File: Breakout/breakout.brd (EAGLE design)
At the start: 53.6 x 40.5 mm, 27 parts, among them U1 TPS63001DRCT, U2 MCP73831

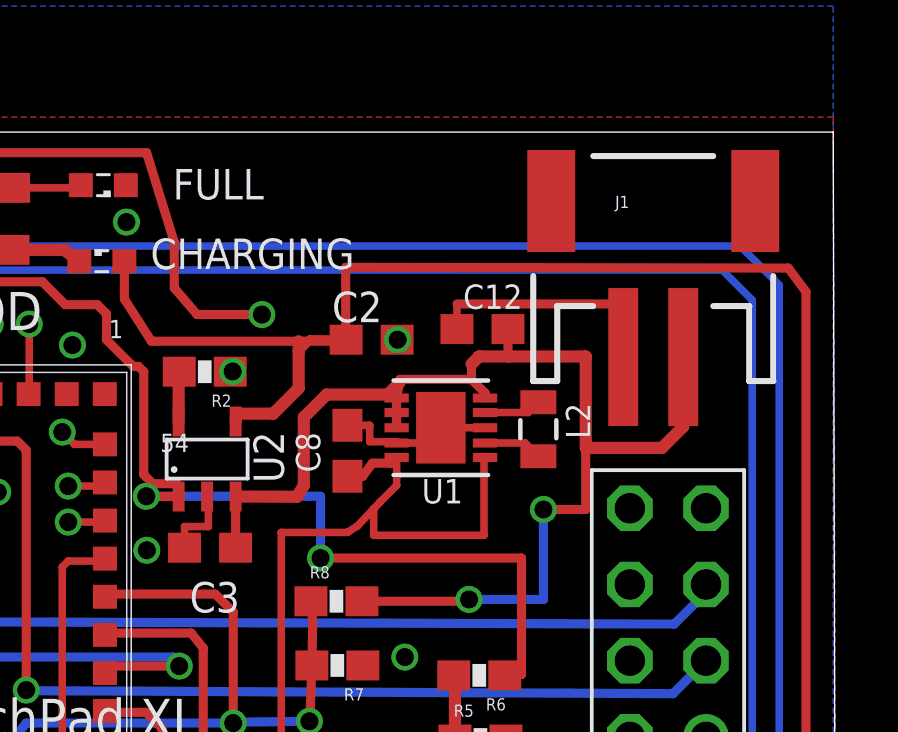
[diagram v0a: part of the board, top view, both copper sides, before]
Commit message: Fixed some pads
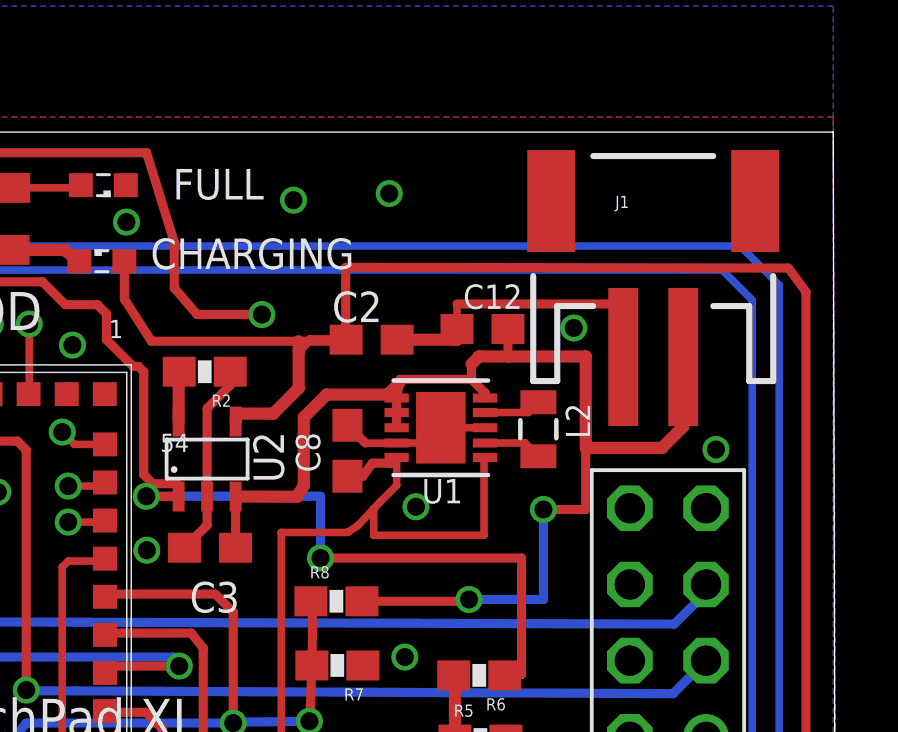
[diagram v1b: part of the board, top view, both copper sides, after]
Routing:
- net GND: track 16.8 -> 22.8 mm, vias 36 -> 39
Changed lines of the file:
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@@
 <layers>
 <layer number="1" name="Top" color="4" fill="1" visible="yes" active="yes"/>
-<layer number="2" name="Route2" color="1" fill="3" visible="yes" active="yes"/>
+<layer number="2" name="Route2" color="1" fill="3" visible="no" active="yes"/>
 <layer number="3" name="Route3" color="4" fill="3" visible="no" active="no"/>
 <layer number="14" name="Route14" color="1" fill="6" visible="no" active="no"/>
-<layer number="15" name="Route15" color="4" fill="6" visible="yes" active="yes"/>
-<layer number="16" name="Bottom" color="1" fill="1" visible="yes" active="yes"/>
+<layer number="15" name="Route15" color="4" fill="6" visible="no" active="yes"/>
+<layer number="16" name="Bottom" color="1" fill="1" visible="no" active="yes"/>
 <layer number="17" name="Pads" color="2" fill="1" visible="yes" active="yes"/>
 <layer number="18" name="Vias" color="2" fill="1" visible="yes" active="yes"/>
@@
 </polygon>
 <contactref element="FULL" pad="C"/>
-<via x="50.88" y="33.58" extent="1-16" drill="0.6"/>
 <via x="42.52" y="26.56" extent="1-16" drill="0.6"/>
 <via x="22.89" y="33.19" extent="1-16" drill="0.6"/>
@@
 <via x="41.84" y="37.5" extent="1-16" drill="0.6"/>
 <via x="37.55" y="28.5" extent="1-16" drill="0.6"/>
-<wire x1="49.206" y1="30.726" x2="49.95" y2="30.726" width="0.254" layer="1"/>
-<wire x1="49.95" y1="30.726" x2="49.95" y2="30.18" width="0.254" layer="1"/>
-<wire x1="49.95" y1="30.18" x2="50.8468" y2="30.18" width="0.254" layer="1"/>
-<wire x1="50.8468" y1="30.18" x2="50.8468" y2="30.136" width="0.254" layer="1"/>
-<via x="45.38" y="32.52" extent="1-16" drill="0.6"/>
 <wire x1="58.4" y1="33" x2="58.39" y2="34.77" width="0.254" layer="1"/>
 <wire x1="58.39" y1="34.77" x2="52.858" y2="34.77" width="0.3048" layer="1"/>
 <wire x1="52.858" y1="34.77" x2="52.858" y2="33.9342" width="0.254" layer="1"/>
-<wire x1="44.53" y1="28.3514" x2="44.57" y2="28.3514" width="0.254" layer="1"/>
-<wire x1="44.57" y1="28.3514" x2="44.57" y2="27.35" width="0.254" layer="1"/>
-<wire x1="44.57" y1="27.35" x2="43.7778" y2="27.35" width="0.254" layer="1"/>
-<wire x1="43.7778" y1="27.35" x2="43.7778" y2="26.6446" width="0.254" layer="1"/>
 <wire x1="53.7932" y1="30.644" x2="52.32" y2="30.644" width="0.254" layer="1"/>
 <via x="51.12" y="23" extent="1-16" drill="0.6"/>
 <contactref element="R5" pad="2"/>
 <contactref element="R7" pad="1"/>
+<wire x1="50.8626" y1="33.5788" x2="52.858" y2="33.5788" width="0.4064" layer="1"/>
+<wire x1="52.858" y1="33.5788" x2="52.858" y2="33.9342" width="0.4064" layer="1"/>
+<wire x1="45.3" y1="32.512" x2="45.3" y2="32.06" width="0.3048" layer="1"/>
+<wire x1="45.3" y1="32.06" x2="44.53" y2="31.29" width="0.3048" layer="1"/>
+<wire x1="44.53" y1="31.29" x2="44.53" y2="28.3514" width="0.3048" layer="1"/>
+<wire x1="49.206" y1="30.726" x2="49.214" y2="30.726" width="0.3048" layer="1"/>
+<wire x1="49.214" y1="30.726" x2="49.81" y2="30.13" width="0.3048" layer="1"/>
+<wire x1="49.81" y1="30.13" x2="50.8208" y2="30.13" width="0.254" layer="1"/>
+<wire x1="50.8208" y1="30.13" x2="50.8468" y2="30.136" width="0.254" layer="1"/>
+<wire x1="44.53" y1="28.3514" x2="44.53" y2="27.3968" width="0.3048" layer="1"/>
+<wire x1="44.53" y1="27.3968" x2="43.7778" y2="26.6446" width="0.3048" layer="1"/>
+<via x="51.49" y="28.01" extent="1-16" drill="0.6"/>
+<via x="56.75" y="33.97" extent="1-16" drill="0.6"/>
+<via x="50.6" y="38.45" extent="1-16" drill="0.6"/>
 <wire x1="41.125" y1="15.72" x2="41.89" y2="15.12" width="0" layer="19" extent="1-1"/>
-<wire x1="49.95" y1="30.726" x2="50.88" y2="33.58" width="0" layer="19" extent="1-1"/>
 <wire x1="53.506" y1="15.748" x2="54.49" y2="20.25" width="0" layer="19" extent="1-1"/>
+<via x="47.41" y="38.23" extent="1-16" drill="0.6"/>
+<via x="61.49" y="29.92" extent="1-16" drill="0.6"/>
 </signal>
 <signal name="N$1">

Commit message: Add Bom file
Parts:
- C1: value (none) -> 1pF
- L1: value (none) -> 3.6nH
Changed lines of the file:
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@@
 <element name="CC3200MOD" library="cc3200mod" package="CC3200MOD" value="CC3200" x="31.6" y="23.74"/>
 <element name="ANT_PAD" library="Antenna" package="ANT" value="ANT" x="24.65" y="0.5"/>
-<element name="C1" library="rcl" package="C0402" value="" x="26.5" y="7.6" smashed="yes">
+<element name="C1" library="rcl" package="C0402" value="1pF" x="26.5" y="7.6" smashed="yes">
 <attribute name="NAME" x="27.7192" y="7.1936" size="1.016" layer="25" font="vector" ratio="18"/>
 <attribute name="VALUE" x="25.865" y="5.695" size="1.27" layer="27"/>
 </element>
-<element name="L1" library="Spark" package="C0402" value="" x="25.9" y="11.3" smashed="yes" rot="R90">
+<element name="L1" library="Spark" package="C0402" value="3.6nH" x="25.9" y="11.3" smashed="yes" rot="R90">
 <attribute name="NAME" x="27.7923" y="11.1984" size="1.016" layer="25" font="vector" ratio="18"/>
 <attribute name="VALUE" x="27.043" y="10.2205" size="0.4064" layer="27" rot="R90"/>

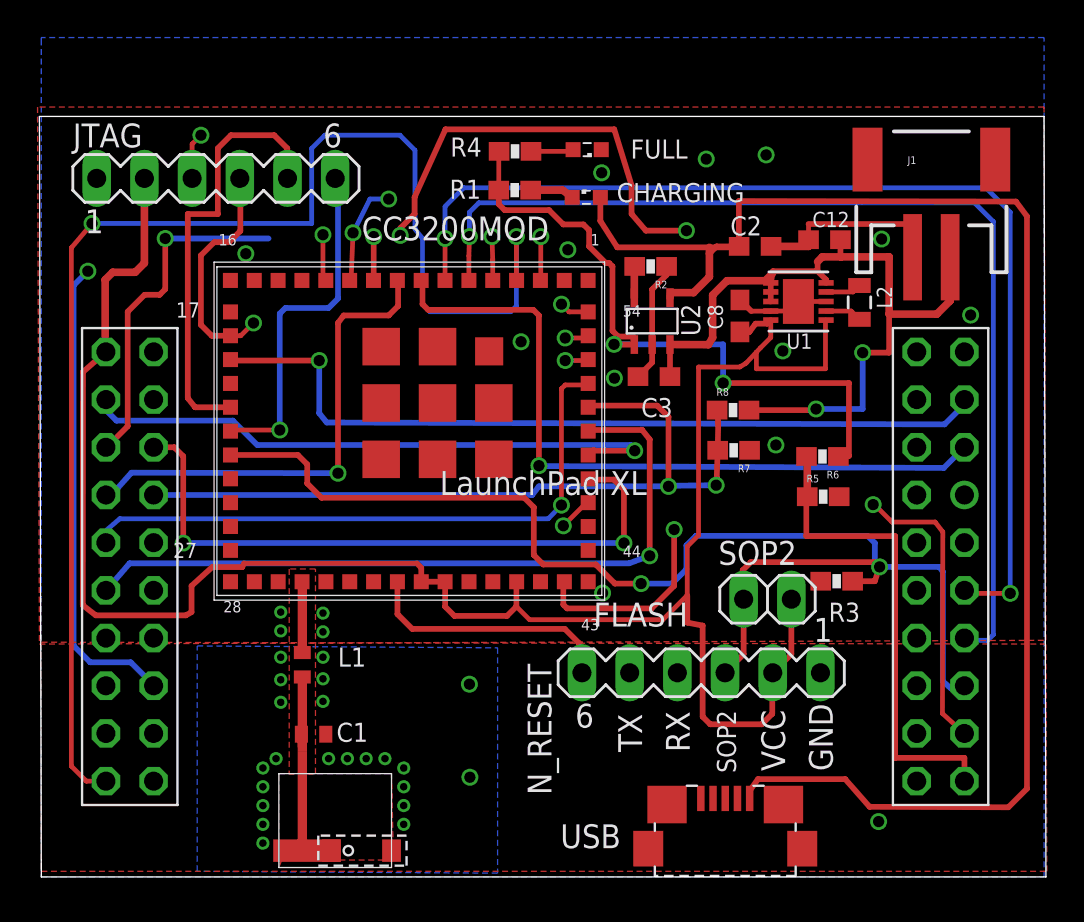
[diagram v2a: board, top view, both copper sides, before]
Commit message: switch charger
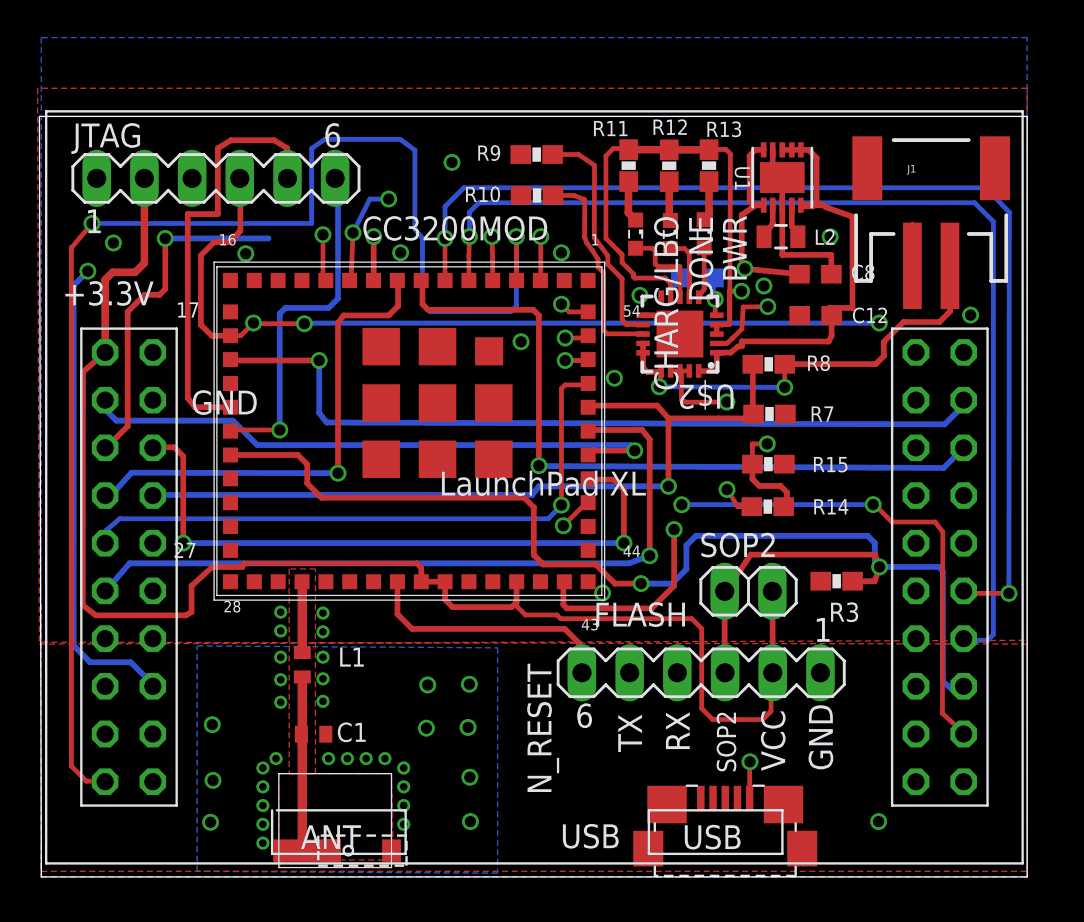
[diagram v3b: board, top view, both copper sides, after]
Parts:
- removed C2, C3: 4.7uF, rcl:C0603
- removed CHARGING, FULL: (no value), eagle-ltspice:LED_SML0603
- removed R1, R4: 470 Ohm, SparkFun-Resistors:0603-RES
- removed R2: 2 k, SparkFun-Resistors:0603-RES
- removed R5, R6: 100K, SparkFun-Resistors:0603-RES
- removed U$1: XL, LaunchPadXL:LAUNCHPADXL
- removed U2: MCP73831, BaseApp:5PIN_SOT23
- added CHARG/LBO: ORANGE, led:SML0603
- added DONE: GREEN, led:SML0603
- added PWR: RED, led:SML0603
- added R10: 100K, SparkFun-Passives:0603-RES
- added R11, R12, R13, R14, R15: 1K, SparkFun-Passives:0603-RES
- added R9: 2K, SparkFun-Passives:0603-RES
- added THERMAL: 10K, SparkFun-Passives:0603-RES
- added U$2: MCP73871-2CCI/ML, microchip-battery:QFN20-4X4
- added U11: XL, LaunchPadXL:LAUNCHPADXL
- moved U1 6.66 mm to (51.5, 37.2), turned to 90 degrees
- moved L2 5.45 mm to (51.4, 34.1), turned to 180 degrees
- moved C8 4.59 mm to (53.2, 32.1), turned to 0 degrees
- moved C12 4.06 mm to (53.2, 29.9)
- moved R8 3.09 mm to (50.7, 27.3)
- moved R7 2.72 mm to (50.8, 24.6)
- moved SOP2 1.09 mm to (49.7, 15.2)
- moved J1 0.46 mm to (59.4, 36.2)
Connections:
- removed net +5V_CHARGE: C2.1, CHARGING.A, U2.P$4, USB.1
- removed net N$7: CHARGING.C, R1.2
- removed net PROG: R2.2, U2.P$5
- removed net STAT: R1.1, R4.1, R6.1, U2.P$1
- new net +5V_USB: R11.2, R12.2, R13.2, R14.2, U$2.17, U$2.18, U$2.19, U$2.3, U$2.4, U$2.9, USB.1
- new net N$17: R9.2, U$2.12
- new net N$20: R10.2, U$2.13
- new net N$26: PWR.A, U$2.6
- new net N$31: DONE.A, U$2.7
- new net N$32: CHARG/LBO.A, U$2.8
- new net N$33: CHARG/LBO.C, R11.1
- new net N$35: DONE.C, R12.1
- new net N$36: PWR.C, R13.1
- new net N$37: R14.1, R15.2, U$2.2
- new net OUT: C12.1, U$2.1, U$2.20, U1.5, U1.6, U1.7, U1.8
- net +BATT: now also U$2.14, U$2.15, U$2.16; no longer C12.1, C3.1, U1.5, U1.6, U1.7, U1.8, U2.P$3
- net GND: now also R10.1, R15.1, R9.1, THERMAL.1, U$2.10, U$2.11, U$2.21, U11.GND1, U11.GND2; no longer C2.2, C3.2, FULL.C, R2.1, R5.2, U$1.GND1, U$1.GND2, U2.P$2
- net GPIO_05: now also U11.GPIO_05; no longer U$1.GPIO_05
- net GPIO_22: now also U11.GPIO_22; no longer R5.1, R6.2, U$1.GPIO_22
- net JTAG_TDI: now also U11.GPIO_23; no longer U$1.GPIO_23
- net JTAG_TDO: now also U11.GPIO_24; no longer U$1.GPIO_24
- net N$10: now also U11.GPIO_16_MOSI; no longer U$1.GPIO_16_MOSI
- net N$11: now also U11.GPIO_17_CS; no longer U$1.GPIO_17_CS
- net N$12: now also U11.GPIO_14_SP_CLK; no longer U$1.GPIO_14_SP_CLK
- net N$13: now also U11.GPIO_28; no longer U$1.GPIO_28
- net N$14: now also U11.GPIO_30; no longer U$1.GPIO_30
- net N$15: now also U11.GPIO_10; no longer U$1.GPIO_10
- net N$16: now also U11.GPIO_11; no longer U$1.GPIO_11
- net N$18: now also U11.GPIO_06; no longer U$1.GPIO_06
- net N$19: now also U11.GPIO_04; no longer U$1.GPIO_04
- net N$21: now also U11.GPIO_07; no longer U$1.GPIO_07
- net N$22: now also U11.GPIO_08; no longer U$1.GPIO_08
- net N$23: now also U11.GPIO_09; no longer U$1.GPIO_09
- net N$24: now also U11.GPIO_13_RX; no longer U$1.GPIO_13_RX
- net N$25: now also U11.GPIO_12_TX; no longer U$1.GPIO_12_TX
- net N$27: now also U11.GPIO_03; no longer U$1.GPIO_03
- net N$28: now also THERMAL.2, U$2.5; no longer FULL.A, R4.2
- net N$8: now also U11.GPIO_15_MISO; no longer U$1.GPIO_15_MISO
- net RX: now also U11.GPIO_01; no longer U$1.GPIO_01
- net SOP2: now also U11.GPIO_25; no longer U$1.GPIO_25
- net TX: now also U11.GPIO_02; no longer U$1.GPIO_02
- net VCC: now also U11.3.3V; no longer U$1.3.3V
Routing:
- net +5V_CHARGE: track 81.0 -> 0.00 mm
- net +5V_USB: track 0.00 -> 65.4 mm, vias 0 -> 4
- net STAT: track 36.4 -> 0.00 mm, vias 2 -> 0
- net GPIO_22: track 94.9 -> 69.2 mm
- net OUT: track 0.00 -> 24.4 mm
- net +BATT: track 41.8 -> 24.1 mm
- net N$37: track 0.00 -> 17.1 mm, vias 0 -> 2
- net N$17: track 0.00 -> 12.4 mm
- net N$20: track 0.00 -> 11.2 mm
- net N$14: track 93.8 -> 85.0 mm
- net GND: track 22.8 -> 14.2 mm, vias 39 -> 44
- net VCC: track 108.7 -> 114.3 mm, vias 0 -> 1
- net N$32: track 0.00 -> 4.78 mm
- net N$31: track 0.00 -> 3.45 mm
- net N$26: track 0.00 -> 2.71 mm
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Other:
- board size 53.6 x 40.5 mm -> 52.6 x 40.5 mm

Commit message: Added FTDI reroute
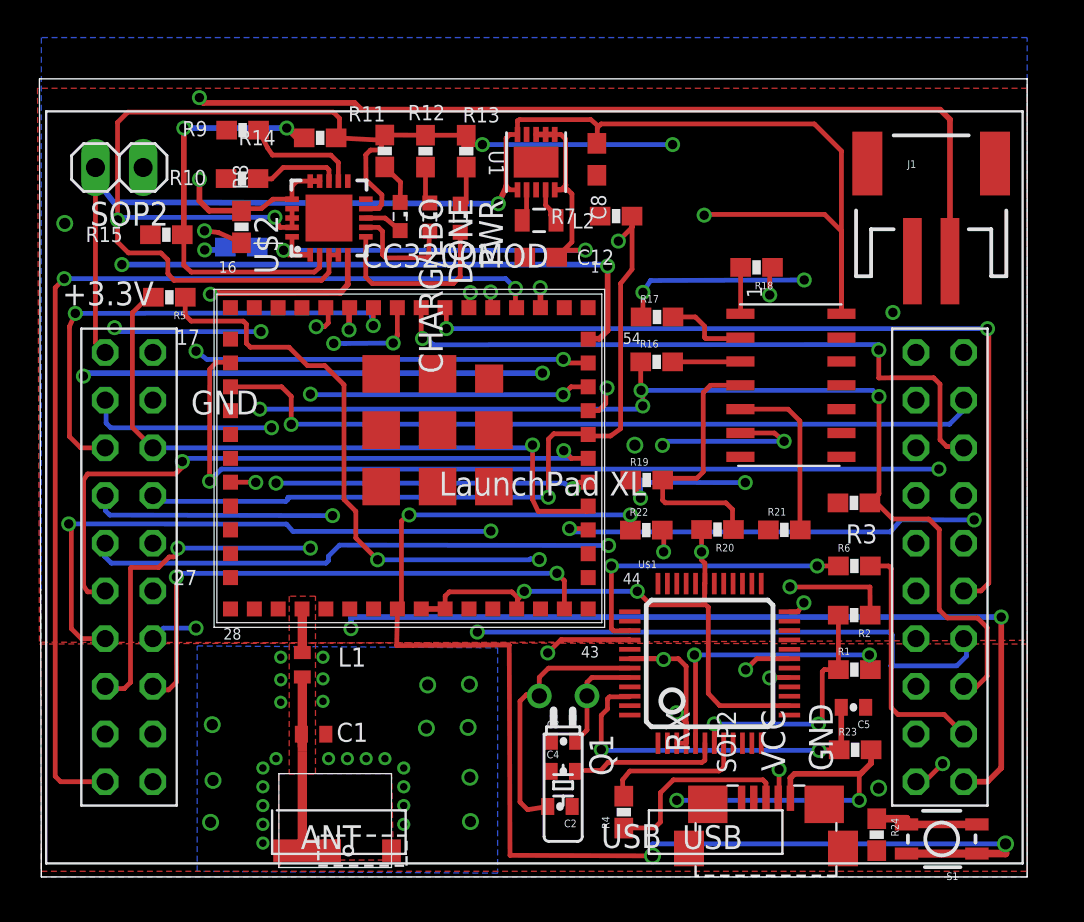
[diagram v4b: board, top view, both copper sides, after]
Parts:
- removed FLASH, JTAG: (no value), con-lstb:MA06-1
- added C2, C3: 27pF, SparkFun-Passives:0402-CAP
- added C4: 33nF, SparkFun-Passives:0402-CAP
- added C5: 0.1uF, SparkFun-Passives:0402-CAP
- added Q1: 16Mhz, crystal:TC26H
- added R1: 1.5K, SparkFun-Resistors:0603-RES
- added R16, R17, R18, R19, R21, R22, R24, R5, R6: 33, SparkFun-Resistors:0603-RES
- added R2, R4: 28, SparkFun-Passives:0603-RES
- added R20: 10k, SparkFun-Resistors:0603-RES
- added R23: 470, SparkFun-Resistors:0603-RES
- added S1: (no value), Spark:TACTILE_SWITCH_SMD
- added U$1: FT2232D, SparkFun-DigitalIC:LQFP-48
- added U$3: DECADE-74LVC125A, DECADE-libraries:DECADE-SO-14
- moved SOP2 40.4 mm to (16.2, 37.8), turned to 180 degrees
- moved R15 34.3 mm to (18.7, 34.2), turned to 0 degrees
- moved R14 30.9 mm to (26.9, 39.4), turned to 0 degrees
- moved R8 29.0 mm to (22.7, 34.6), turned to 90 degrees
- moved THERMAL 24.3 mm to (22.6, 33.5), turned to 0 degrees
- moved U$2 19.7 mm to (27.3, 35.1), turned to 90 degrees
- moved R10 15.7 mm to (22.7, 37.2)
- moved R9 15.7 mm to (22.7, 39.8)
- moved C12 15.0 mm to (38.6, 33.0)
- moved R7 13.3 mm to (42.6, 35.2), turned to 0 degrees
- moved C8 13.2 mm to (41.6, 38.2), turned to 270 degrees
- moved U1 13.1 mm to (38.4, 38.1)
- moved PWR 13.0 mm to (34.3, 35.1)
- moved R11 13.0 mm to (30.3, 38.7)
- moved R12 13.0 mm to (32.5, 38.6)
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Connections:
- removed net JTAG_TCK: CC3200MOD.P21, JTAG.5
- removed net JTAG_TMS: CC3200MOD.P22, JTAG.6
- removed net RX: CC3200MOD.P46, FLASH.4, U11.GPIO_01
- removed net TX: CC3200MOD.P47, FLASH.5, U11.GPIO_02
- new net DBGEN_N: R18.2, U$3.1
- new net DBG_RST_N: R19.2, R20.1, U$3.4
- new net FTDI_RX: CC3200MOD.P46, R6.2, U11.GPIO_01
- new net FTDI_TX: CC3200MOD.P47, R5.2, U11.GPIO_02
- new net FT_SK: R17.2, U$3.2
- new net N$38: C2.2, Q1.2, U$1.43
- new net N$39: USB.4
- new net N$40: C3.2, Q1.1, U$1.44
- new net N$41: R4.1, USB.3
- new net N$42: R2.1, USB.2
- new net N$43: C4.2, U$1.6
- new net N$44: R5.1, U$1.40
- new net N$45: R6.1, U$1.39
- new net N$46: R17.1, U$1.24
- new net N$47: R19.1, U$1.19
- new net N$48: R18.1, U$1.17
- new net N$49: R21.2, U$3.5
- new net N$50: R22.2, U$3.6
- new net N$51: C5.2, R23.1, U$1.46
- new net N$53: R24.1, S1.3, S1.4
- new net N$7: R1.2, U$1.5
- new net TCK: R16.2, U$3.3
- new net USB_DM: R4.2, U$1.8
- new net USB_DP: R1.1, R2.2, U$1.7
- net +5V_USB: now also R23.2, U$1.3, U$1.4, U$1.42
- net GND: now also C2.1, C3.1, C4.1, C5.1, R21.1, R24.2, U$1.18, U$1.25, U$1.34, U$1.45, U$1.47, U$1.9, U$3.7; no longer FLASH.1, JTAG.1
- net JTAG_TDI: no longer JTAG.3
- net JTAG_TDO: no longer JTAG.4
- net N_RESET: now also R22.1, S1.1, S1.2; no longer FLASH.6
- net SOP2: now also R16.1; no longer FLASH.3
- net VCC: now also R20.2, U$1.14, U$1.31, U$3.14; no longer FLASH.2, JTAG.2
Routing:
- net +5V_USB: track 65.4 -> 132.1 mm, vias 4 -> 8
- net N_RESET: track 13.7 -> 73.6 mm, vias 0 -> 4
- net RX: track 57.5 -> 0.00 mm, vias 3 -> 0
- net N$14: track 85.0 -> 29.6 mm, vias 4 -> 2
- net FTDI_RX: track 0.00 -> 48.7 mm, vias 0 -> 2
- net TX: track 41.9 -> 0.00 mm, vias 2 -> 0
- net N$44: track 0.00 -> 40.1 mm, vias 0 -> 3
- net +BATT: track 24.1 -> 61.2 mm
- net FTDI_TX: track 0.00 -> 36.0 mm, vias 0 -> 1
- net N$46: track 0.00 -> 28.5 mm, vias 0 -> 3
- net N$48: track 0.00 -> 23.0 mm, vias 0 -> 2
- net JTAG_TCK: track 23.0 -> 0.00 mm
- net GPIO_05: track 43.2 -> 66.1 mm, vias 1 -> 3
- net N$47: track 0.00 -> 20.4 mm, vias 0 -> 3
- net JTAG_TDI: track 76.0 -> 56.1 mm, vias 1 -> 2
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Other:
- board size 52.6 x 40.5 mm -> 52.6 x 42.5 mm
- board text removed: "N_RESET"
- board text removed: "TX"
